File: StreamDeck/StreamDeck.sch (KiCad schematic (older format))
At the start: 47 parts, among them IC1 ATMEGA48V-10PU, J1 DISPLAY1, J2 DISPLAY2, J3 DISPLAY3, J4 DISPLAY4, J5 DISPLAY5, J6 DISPLAY6, J7 DISPLAY7, J8 DISPLAY8, J9 sd_CARD_READER_MODULE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

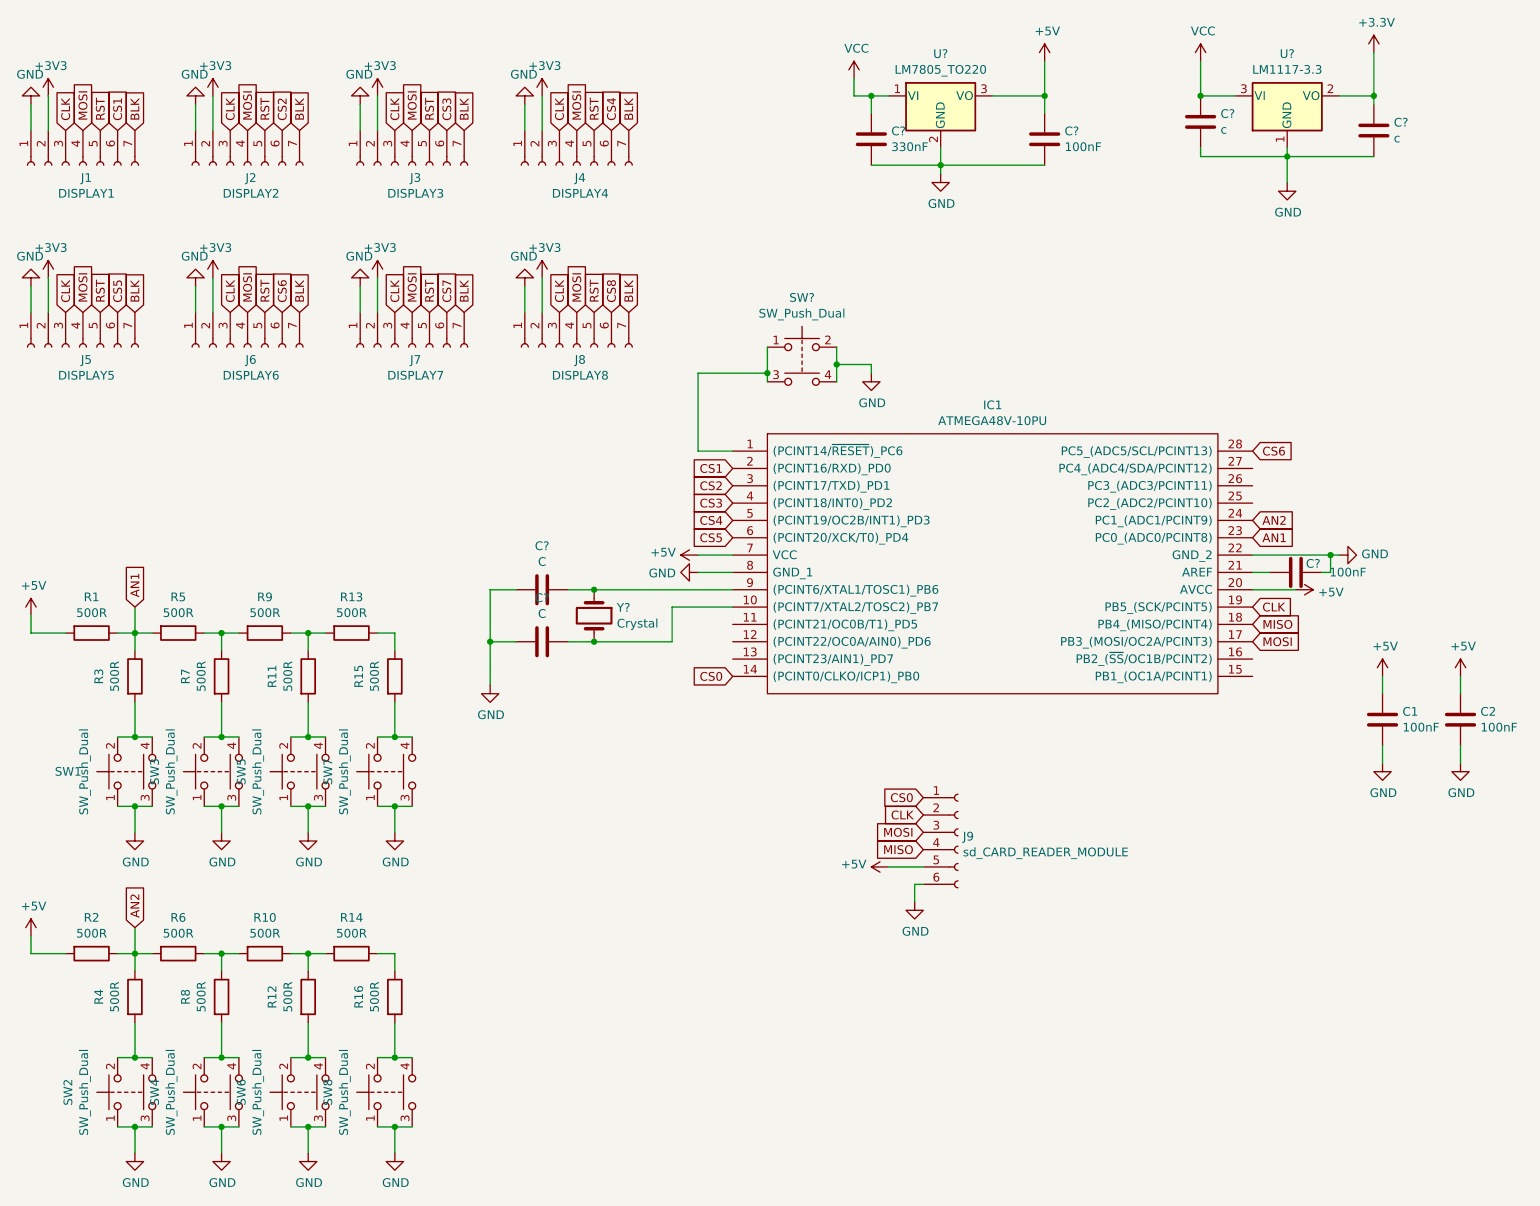
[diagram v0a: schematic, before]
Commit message: Upgrade schematic e segmentação dos subcircuitos
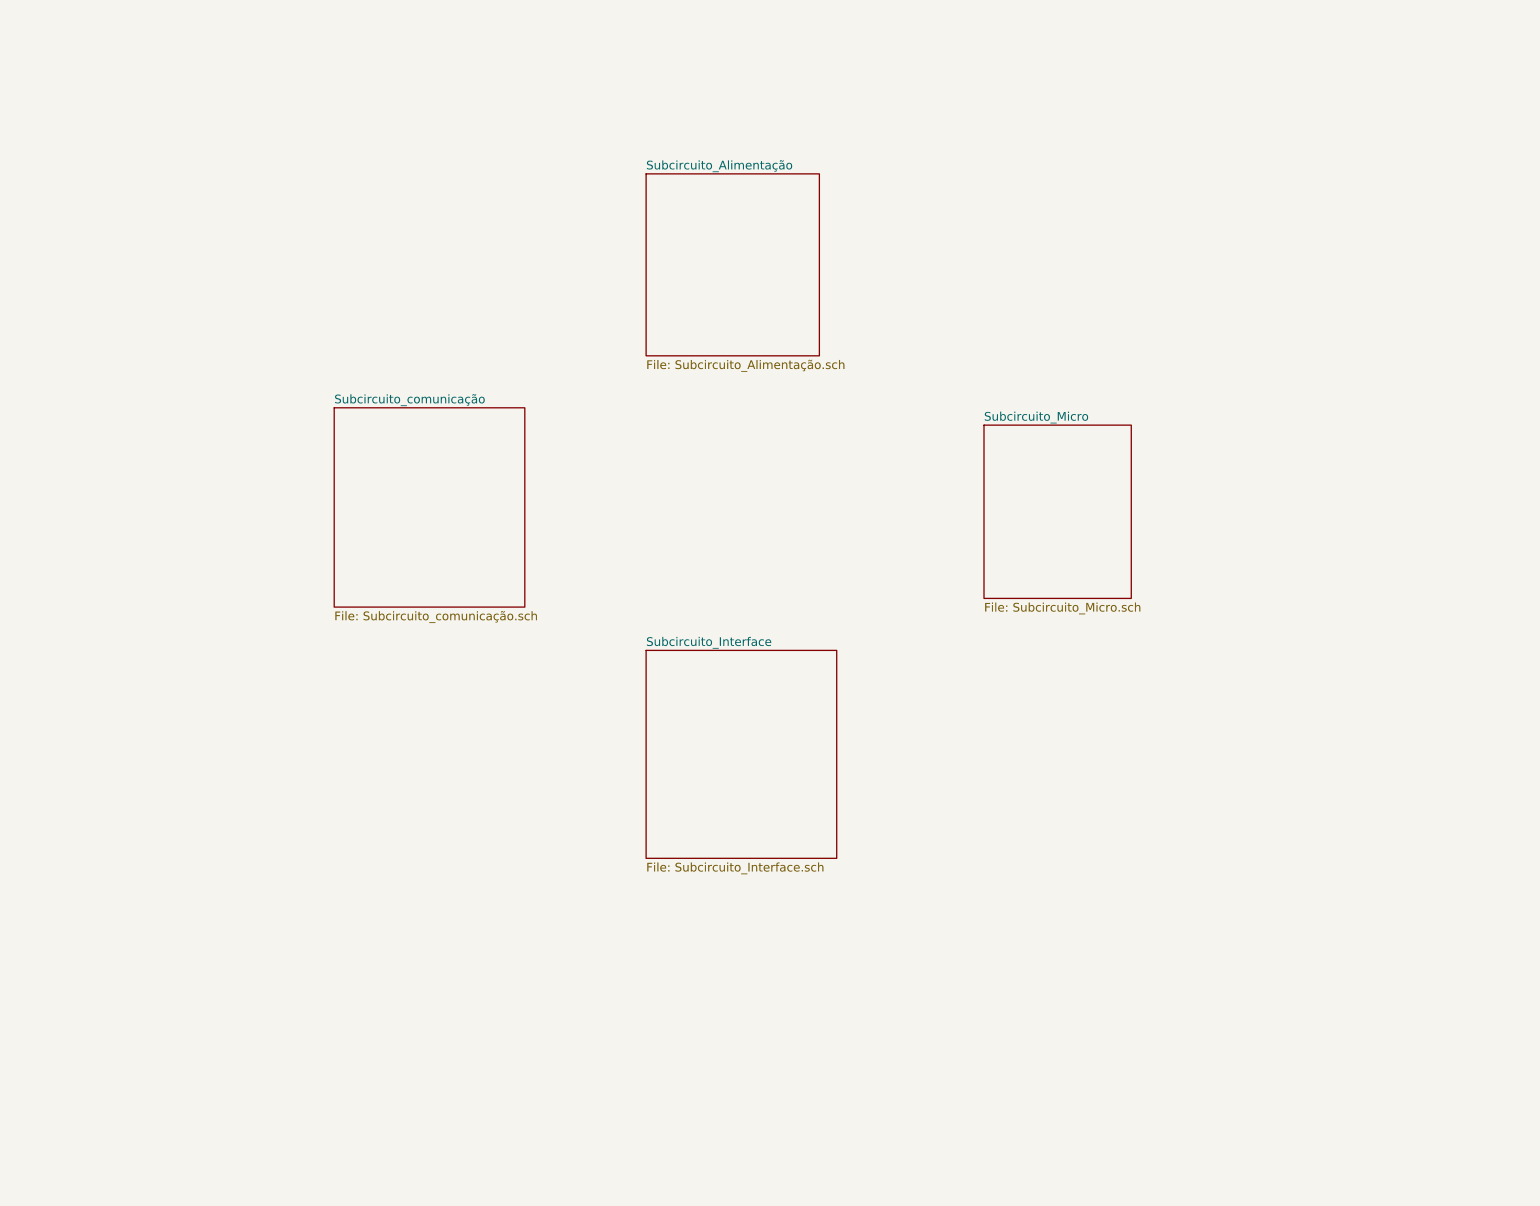
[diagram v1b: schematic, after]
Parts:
- removed C1, C2, C? (x2): 100nF, symbol Device:C
- removed C?: 330nF, symbol Device:C
- removed C? (x2): c, symbol Device:C
- removed C? (x2): C, symbol Device:C
- removed IC1: ATMEGA48V-10PU, DIP794W53P254L3467H457Q28N, symbol SamacSys_Parts:ATMEGA48V-10PU
- removed J1: DISPLAY1, symbol Connector:Conn_01x07_Female
- removed J2: DISPLAY2, symbol Connector:Conn_01x07_Female
- removed J3: DISPLAY3, symbol Connector:Conn_01x07_Female
- removed J4: DISPLAY4, symbol Connector:Conn_01x07_Female
- removed J5: DISPLAY5, symbol Connector:Conn_01x07_Female
- removed J6: DISPLAY6, symbol Connector:Conn_01x07_Female
- removed J7: DISPLAY7, symbol Connector:Conn_01x07_Female
- removed J8: DISPLAY8, symbol Connector:Conn_01x07_Female
- removed J9: sd_CARD_READER_MODULE, symbol Connector:Conn_01x06_Female
- removed R1, R10, R11, R12, R13, R14, R15, R16, R2, R3, R4, R5, R6, R7, R8, R9: 500R, symbol Device:R
- removed SW1, SW2, SW3, SW4, SW5, SW6, SW7, SW8, SW?: SW_Push_Dual, symbol Switch:SW_Push_Dual
- removed U?: LM7805_TO220, Package_TO_SOT_THT:TO-220-3_Vertical, symbol Regulator_Linear:LM7805_TO220
- removed U?: LM1117-3.3, symbol Regulator_Linear:LM1117-3.3
- removed Y?: Crystal, symbol Device:Crystal
